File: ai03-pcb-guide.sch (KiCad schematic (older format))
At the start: 24 parts, among them SW1 SW_Push, U1 ATmega32U4-AU, Y1 16MHz

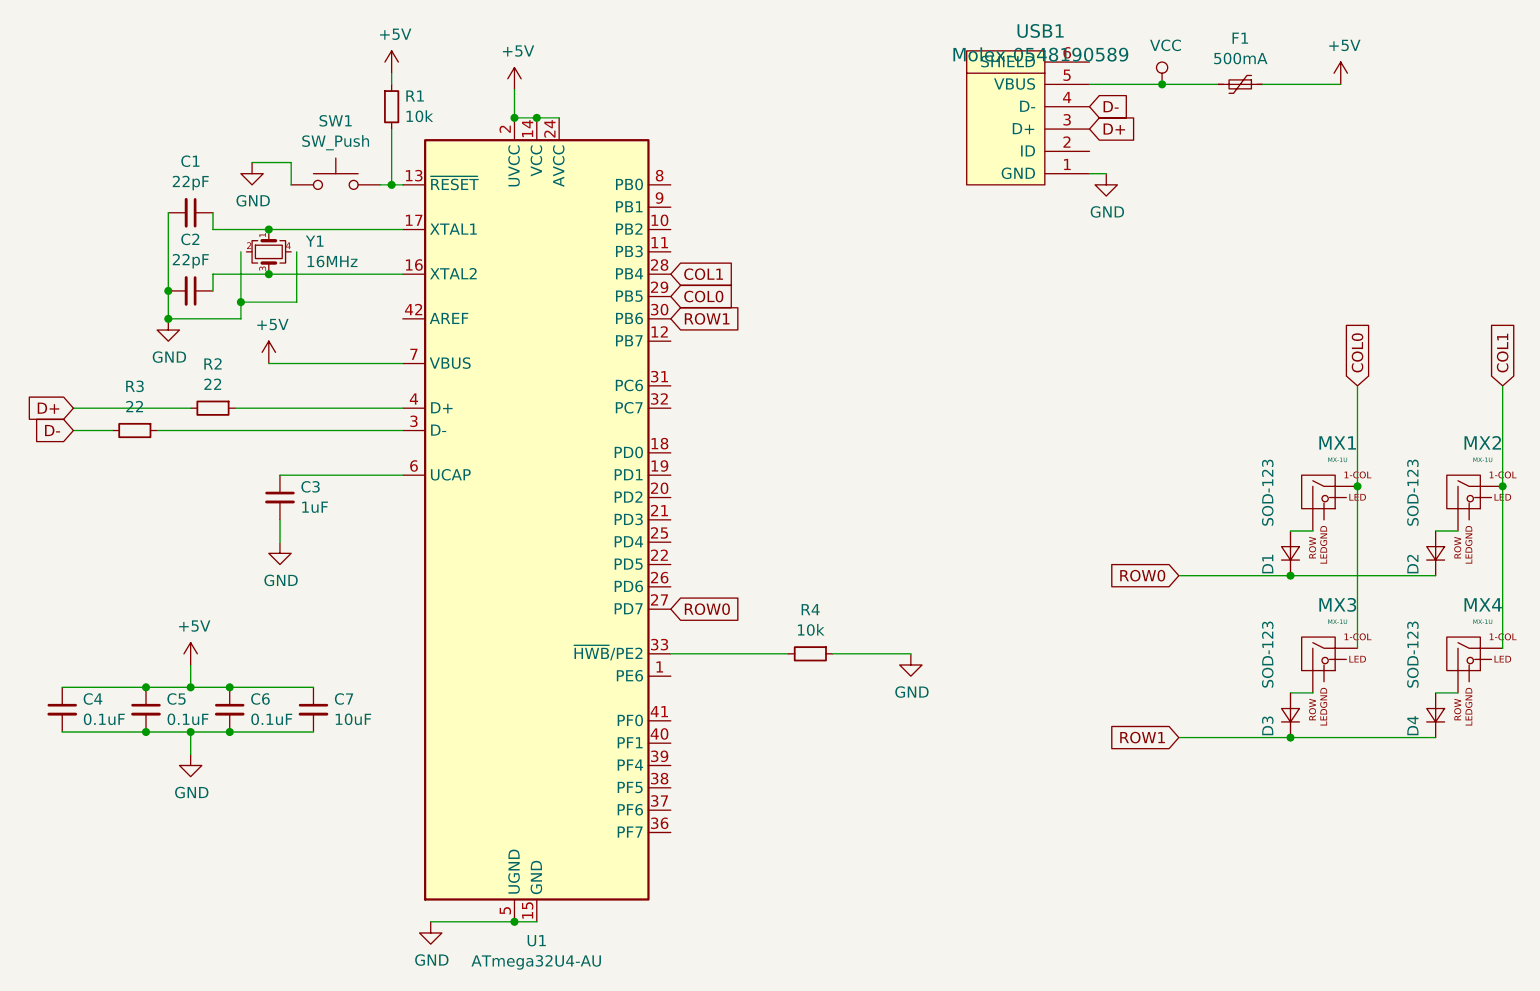
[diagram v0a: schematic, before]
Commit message: Update to KiCad 5.1.2 guide data
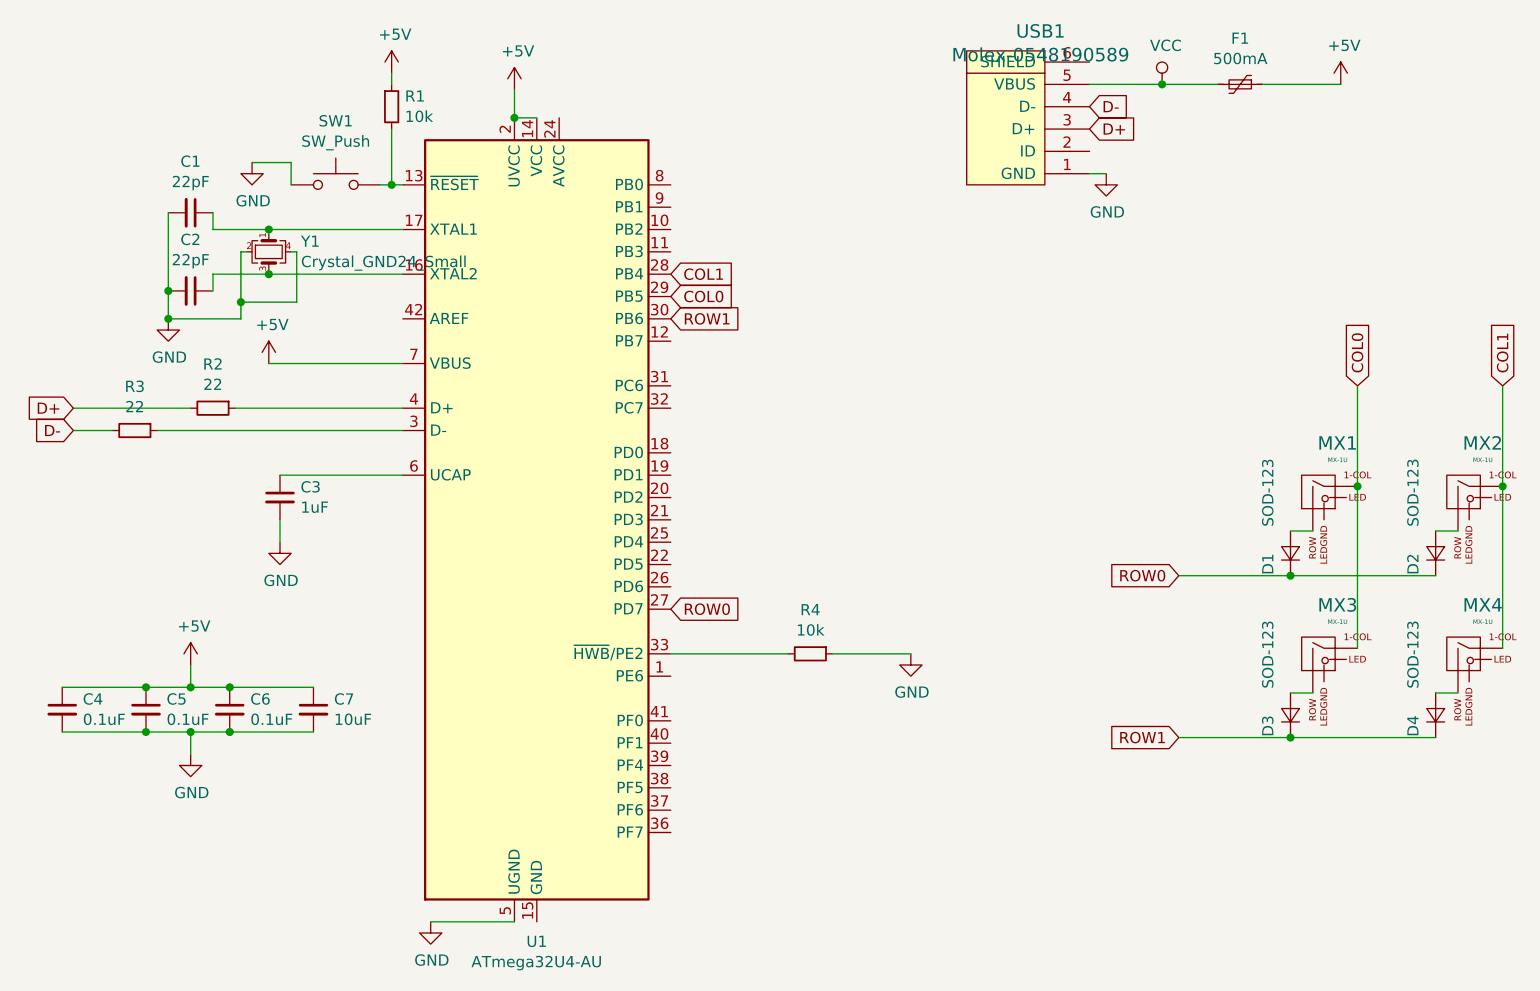
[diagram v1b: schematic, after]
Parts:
- Y1: value 16MHz -> Crystal_GND24_Small
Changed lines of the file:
@@
 EESchema Schematic File Version 4
-EELAYER 26 0
+LIBS:ai03-pcb-guide-cache
+EELAYER 29 0
 EELAYER END
 $Descr A4 11693 8268
@@
 $EndDescr
 $Comp
-L MCU_Microchip_ATmega:ATmega32U4-AU U1
-U 1 1 5C33F15A
-P 3650 3625
-F 0 "U1" H 3650 1739 50  0000 C CNN
-F 1 "ATmega32U4-AU" H 3650 1648 50  0000 C CNN
-F 2 "Housings_QFP:TQFP-44_10x10mm_Pitch0.8mm" H 3650 3625 50  0001 C CIN
-F 3 "http://ww1.microchip.com/downloads/en/DeviceDoc/Atmel-7766-8-bit-AVR-ATmega16U4-32U4_Datasheet.pdf" H 3650 3625 50  0001 C CNN
-	1    3650 3625
-	1    0    0    -1
-$EndComp
-$Comp
 L power:+5V #PWR0101
 U 1 1 5C33F300
@@
 Wire Wire Line
 	3550 1700 3550 1825
-Wire Wire Line
-	3550 1825 3650 1825
-Connection ~ 3550 1825
-Connection ~ 3650 1825
-Wire Wire Line
-	3650 1825 3750 1825
 $Comp
 L power:GND #PWR0102
@@
 	1    0    0    -1
 $EndComp
-Wire Wire Line
-	3175 5425 3550 5425
-Connection ~ 3550 5425
-Wire Wire Line
-	3550 5425 3650 5425
 $Comp
 L Device:R_Small R4
@@
 	2450 2925 3050 2925
 $Comp
-L Device:Crystal_GND24_Small Y1
-U 1 1 5C341379
-P 2450 2425
-F 0 "Y1" V 2404 2591 50  0000 L CNN
-F 1 "16MHz" V 2495 2591 50  0000 L CNN
-F 2 "Crystals:Crystal_SMD_3225-4pin_3.2x2.5mm" H 2450 2425 50  0001 C CNN
-F 3 "~" H 2450 2425 50  0001 C CNN
-	1    2450 2425
-	0    1    1    0
-$EndComp
-Wire Wire Line
-	2450 2325 3050 2325
-Wire Wire Line
-	3050 2525 2450 2525
-$Comp
 L Device:C_Small C1
 U 1 1 5C341D22
@@
 $EndComp
 Wire Wire Line
-	2450 2325 2200 2325
-Wire Wire Line
 	2200 2325 2200 2250
-Connection ~ 2450 2325
-Wire Wire Line
-	2450 2525 2200 2525
 Wire Wire Line
 	2200 2525 2200 2600
-Connection ~ 2450 2525
 $Comp
 L power:GND #PWR0108
@@
 Text GLabel 4250 2725 2    50   Input ~ 0
 ROW1
+Wire Wire Line
+	2550 2425 2575 2425
+Wire Wire Line
+	2350 2425 2325 2425
+$Comp
+L MCU_Microchip_ATmega:ATmega32U4-AU U1
+U 1 1 5CEB8A23
+P 3650 3625
+F 0 "U1" H 3650 1736 50  0000 C CNN
+F 1 "ATmega32U4-AU" H 3650 1645 50  0000 C CNN
+F 2 "Housings_QFP:TQFP-44_10x10mm_Pitch0.8mm" H 3650 3625 50  0001 C CIN
+F 3 "http://ww1.microchip.com/downloads/en/DeviceDoc/Atmel-7766-8-bit-AVR-ATmega16U4-32U4_Datasheet.pdf" H 3650 3625 50  0001 C CNN
+	1    3650 3625
+	1    0    0    -1
+$EndComp
+Wire Wire Line
+	3550 1825 3650 1825
+Wire Wire Line
+	3175 5425 3550 5425
+Connection ~ 3550 1825
+Wire Wire Line
+	2200 2325 2450 2325
+Wire Wire Line
+	2200 2525 2450 2525
+$Comp
+L Device:Crystal_GND24_Small Y1
+U 1 1 5CEBCEA8
+P 2450 2425
+F 0 "Y1" V 2404 2569 50  0000 L CNN
+F 1 "Crystal_GND24_Small" V 2495 2569 50  0000 L CNN
+F 2 "Crystals:Crystal_SMD_3225-4pin_3.2x2.5mm" H 2450 2425 50  0001 C CNN
+F 3 "~" H 2450 2425 50  0001 C CNN
+	1    2450 2425
+	0    1    1    0
+$EndComp
+Connection ~ 2450 2525
+Wire Wire Line
+	2450 2525 3050 2525
+Connection ~ 2450 2325
+Wire Wire Line
+	2450 2325 3050 2325
 $EndSCHEMATC

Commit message: Progress
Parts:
- removed MX1, MX2, MX3, MX4: MX-1U, MX_Alps_Hybrid:MX-1U, symbol MX_Alps_Hybrids:MX-1U
- added MX? (x4): MX-NoLED, symbol MX_Alps_Hybrid:MX-NoLED
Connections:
- net COL0: now also MX?.1 (COL), MX?.1 (COL)
- net COL1: now also MX?.1 (COL), MX?.1 (COL)
- net at D1.2 (A): now also MX?.2 (ROW)
- net at D2.2 (A): now also MX?.2 (ROW)
- net at D3.2 (A): now also MX?.2 (ROW)
- net at D4.2 (A): now also MX?.2 (ROW)
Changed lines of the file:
@@
 	6200 2075 6125 2075
-$Comp
-L MX_Alps_Hybrids:MX-1U MX1
-U 1 1 5C34B436
-P 7150 3500
-F 0 "MX1" H 7236 3717 60  0000 C CNN
-F 1 "MX-1U" H 7236 3643 20  0000 C CNN
-F 2 "MX_Alps_Hybrid:MX-1U" H 7125 3475 60  0001 C CNN
-F 3 "" H 7125 3475 60  0001 C CNN
-	1    7150 3500
-	1    0    0    -1
-$EndComp
 $Comp
 L Device:D_Small D1
@@
 	7025 3675 7125 3675
 $Comp
-L MX_Alps_Hybrids:MX-1U MX2
-U 1 1 5C34C49C
-P 7800 3500
-F 0 "MX2" H 7886 3717 60  0000 C CNN
-F 1 "MX-1U" H 7886 3643 20  0000 C CNN
-F 2 "MX_Alps_Hybrid:MX-1U" H 7775 3475 60  0001 C CNN
-F 3 "" H 7775 3475 60  0001 C CNN
-	1    7800 3500
-	1    0    0    -1
-$EndComp
-$Comp
 L Device:D_Small D2
 U 1 1 5C34C4A3
@@
 	7675 3675 7775 3675
 $Comp
-L MX_Alps_Hybrids:MX-1U MX3
-U 1 1 5C34D1F8
-P 7150 4225
-F 0 "MX3" H 7236 4442 60  0000 C CNN
-F 1 "MX-1U" H 7236 4368 20  0000 C CNN
-F 2 "MX_Alps_Hybrid:MX-1U" H 7125 4200 60  0001 C CNN
-F 3 "" H 7125 4200 60  0001 C CNN
-	1    7150 4225
-	1    0    0    -1
-$EndComp
-$Comp
 L Device:D_Small D3
 U 1 1 5C34D1FF
@@
 Wire Wire Line
 	7025 4400 7125 4400
-$Comp
-L MX_Alps_Hybrids:MX-1U MX4
-U 1 1 5C34D207
-P 7800 4225
-F 0 "MX4" H 7886 4442 60  0000 C CNN
-F 1 "MX-1U" H 7886 4368 20  0000 C CNN
-F 2 "MX_Alps_Hybrid:MX-1U" H 7775 4200 60  0001 C CNN
-F 3 "" H 7775 4200 60  0001 C CNN
-	1    7800 4225
-	1    0    0    -1
-$EndComp
 $Comp
 L Device:D_Small D4
@@
 Wire Wire Line
 	7025 4600 6525 4600
-Wire Wire Line
-	7325 4200 7325 3475
-Connection ~ 7325 3475
-Wire Wire Line
-	7325 3475 7325 3025
-Wire Wire Line
-	7975 4200 7975 3475
-Connection ~ 7975 3475
-Wire Wire Line
-	7975 3475 7975 3025
 Text GLabel 7325 3025 1    50   Input ~ 0
 COL0
@@
 Wire Wire Line
 	2450 2325 3050 2325
+Wire Wire Line
+	7325 3025 7325 3475
+Wire Wire Line
+	7975 3025 7975 3475
+$Comp
+L MX_Alps_Hybrid:MX-NoLED MX?
+U 1 1 5D099790
+P 7175 3525
+F 0 "MX?" H 7208 3748 60  0000 C CNN
+F 1 "MX-NoLED" H 7208 3674 20  0000 C CNN
+F 2 "" H 6550 3500 60  0001 C CNN
+F 3 "" H 6550 3500 60  0001 C CNN
+	1    7175 3525
+	1    0    0    -1
+$EndComp
+Connection ~ 7325 3475
+Wire Wire Line
+	7325 3475 7325 4200
+$Comp
+L MX_Alps_Hybrid:MX-NoLED MX?
+U 1 1 5D09A176
+P 7825 3525
+F 0 "MX?" H 7858 3748 60  0000 C CNN
+F 1 "MX-NoLED" H 7858 3674 20  0000 C CNN
+F 2 "" H 7200 3500 60  0001 C CNN
+F 3 "" H 7200 3500 60  0001 C CNN
+	1    7825 3525
+	1    0    0    -1
+$EndComp
+Connection ~ 7975 3475
+Wire Wire Line
+	7975 3475 7975 4200
+$Comp
+L MX_Alps_Hybrid:MX-NoLED MX?
+U 1 1 5D09AA2F
+P 7175 4250
+F 0 "MX?" H 7208 4473 60  0000 C CNN
+F 1 "MX-NoLED" H 7208 4399 20  0000 C CNN
+F 2 "" H 6550 4225 60  0001 C CNN
+F 3 "" H 6550 4225 60  0001 C CNN
+	1    7175 4250
+	1    0    0    -1
+$EndComp
+$Comp
+L MX_Alps_Hybrid:MX-NoLED MX?
+U 1 1 5D09B9B4
+P 7825 4250
+F 0 "MX?" H 7858 4473 60  0000 C CNN
+F 1 "MX-NoLED" H 7858 4399 20  0000 C CNN
+F 2 "" H 7200 4225 60  0001 C CNN
+F 3 "" H 7200 4225 60  0001 C CNN
+	1    7825 4250
+	1    0    0    -1
+$EndComp
 $EndSCHEMATC

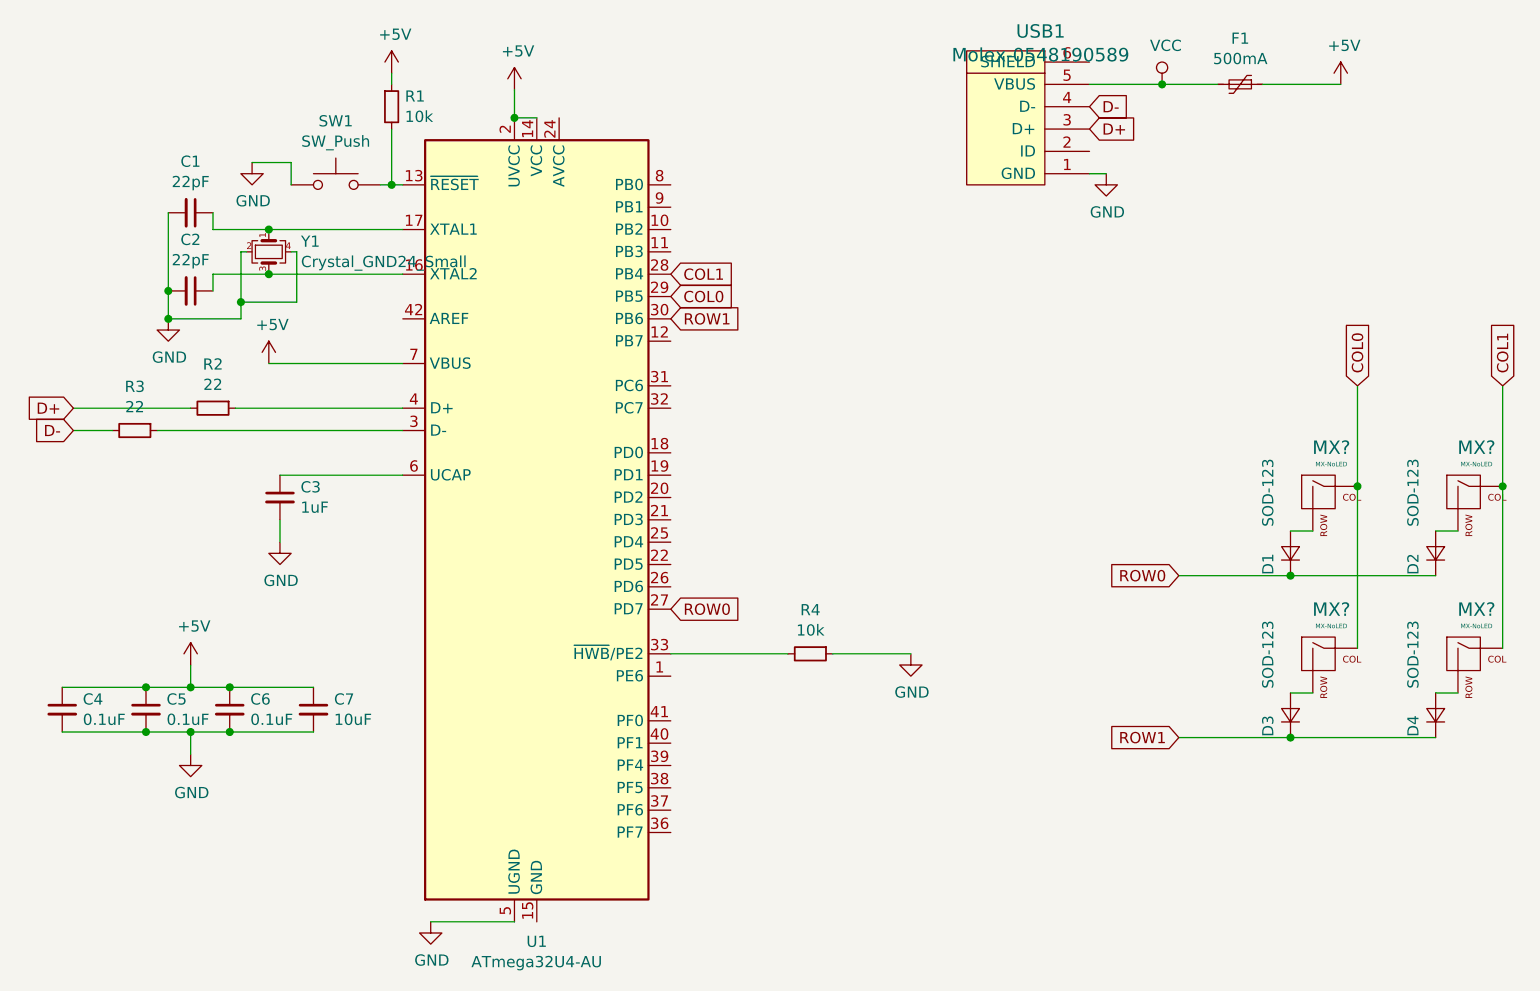
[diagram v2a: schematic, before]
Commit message: Update PCB for revised guide
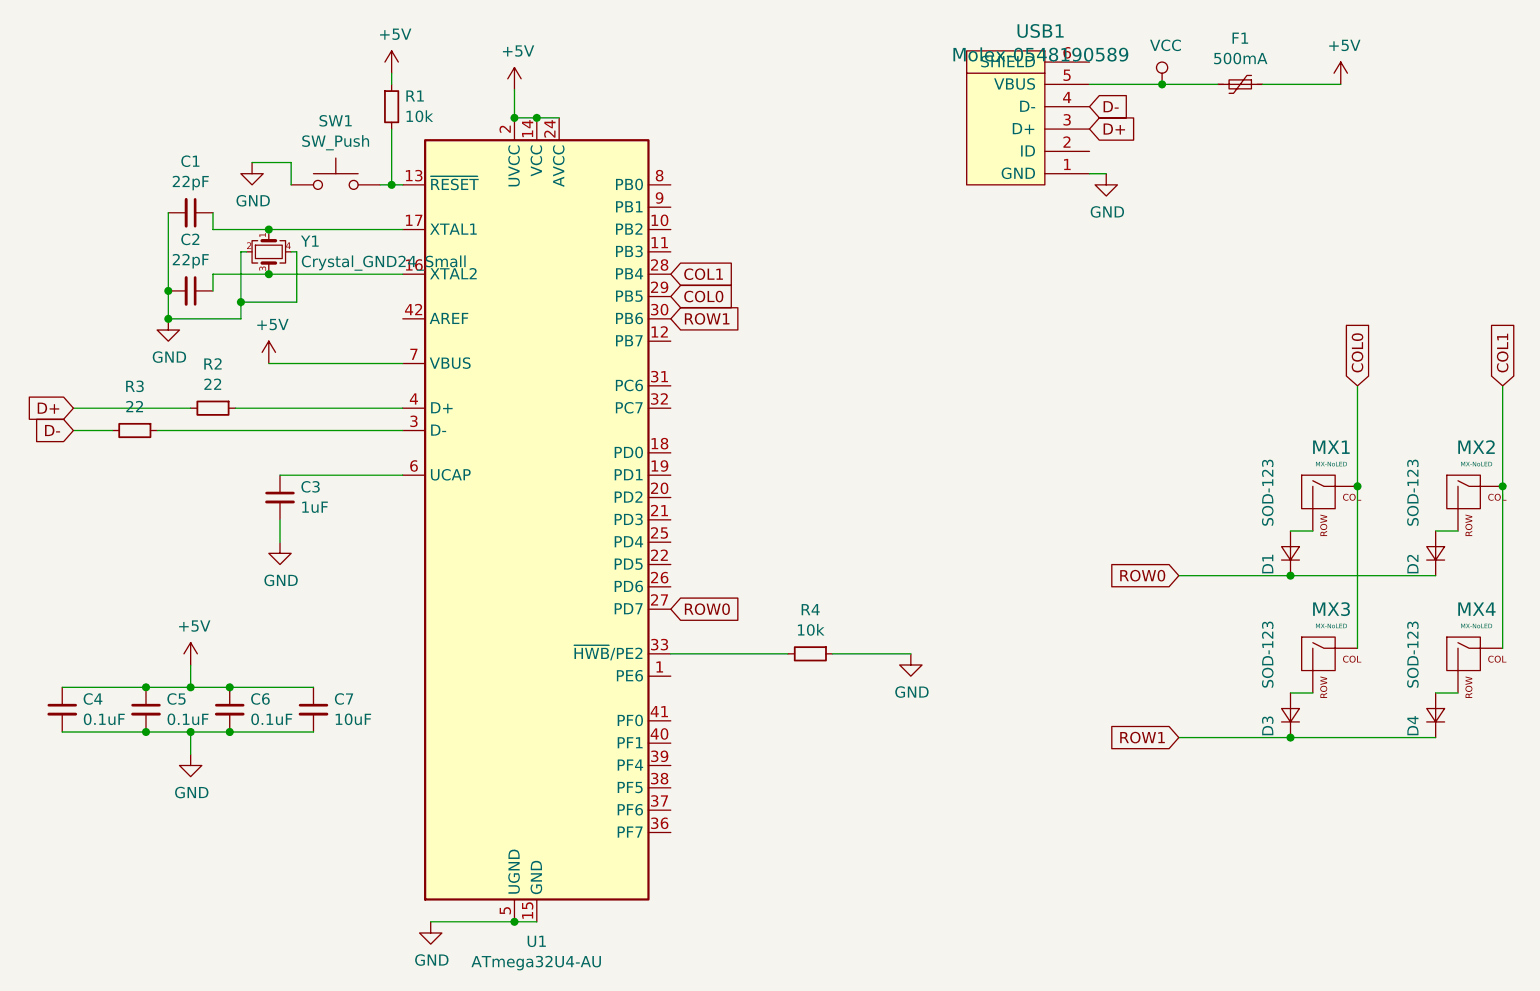
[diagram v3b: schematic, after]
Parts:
- MX1, MX2, MX3, MX4: renamed from MX?; footprint (none) -> MX_Alps_Hybrid:MX-1U
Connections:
- net +5V: now also U1.24 (AVCC), U1.44 (AVCC)
- net GND: now also U1.15 (GND), U1.23 (GND), U1.35 (GND), U1.43 (GND)
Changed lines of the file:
@@
 Wire Wire Line
 	7675 3875 7025 3875
-Connection ~ 7025 3875
 Wire Wire Line
 	7025 3875 6525 3875
 Wire Wire Line
 	7675 4600 7025 4600
-Connection ~ 7025 4600
 Wire Wire Line
 	7025 4600 6525 4600
@@
 	7975 3025 7975 3475
 $Comp
-L MX_Alps_Hybrid:MX-NoLED MX?
+L MX_Alps_Hybrid:MX-NoLED MX1
 U 1 1 5D099790
 P 7175 3525
-F 0 "MX?" H 7208 3748 60  0000 C CNN
+F 0 "MX1" H 7208 3748 60  0000 C CNN
 F 1 "MX-NoLED" H 7208 3674 20  0000 C CNN
-F 2 "" H 6550 3500 60  0001 C CNN
+F 2 "MX_Alps_Hybrid:MX-1U" H 6550 3500 60  0001 C CNN
 F 3 "" H 6550 3500 60  0001 C CNN
 	1    7175 3525
 	1    0    0    -1
 $EndComp
-Connection ~ 7325 3475
 Wire Wire Line
 	7325 3475 7325 4200
 $Comp
-L MX_Alps_Hybrid:MX-NoLED MX?
+L MX_Alps_Hybrid:MX-NoLED MX2
 U 1 1 5D09A176
 P 7825 3525
-F 0 "MX?" H 7858 3748 60  0000 C CNN
+F 0 "MX2" H 7858 3748 60  0000 C CNN
 F 1 "MX-NoLED" H 7858 3674 20  0000 C CNN
-F 2 "" H 7200 3500 60  0001 C CNN
+F 2 "MX_Alps_Hybrid:MX-1U" H 7200 3500 60  0001 C CNN
 F 3 "" H 7200 3500 60  0001 C CNN
 	1    7825 3525
 	1    0    0    -1
 $EndComp
-Connection ~ 7975 3475
 Wire Wire Line
 	7975 3475 7975 4200
 $Comp
-L MX_Alps_Hybrid:MX-NoLED MX?
+L MX_Alps_Hybrid:MX-NoLED MX3
 U 1 1 5D09AA2F
 P 7175 4250
-F 0 "MX?" H 7208 4473 60  0000 C CNN
+F 0 "MX3" H 7208 4473 60  0000 C CNN
 F 1 "MX-NoLED" H 7208 4399 20  0000 C CNN
-F 2 "" H 6550 4225 60  0001 C CNN
+F 2 "MX_Alps_Hybrid:MX-1U" H 6550 4225 60  0001 C CNN
 F 3 "" H 6550 4225 60  0001 C CNN
 	1    7175 4250
@@
 $EndComp
 $Comp
-L MX_Alps_Hybrid:MX-NoLED MX?
+L MX_Alps_Hybrid:MX-NoLED MX4
 U 1 1 5D09B9B4
 P 7825 4250
-F 0 "MX?" H 7858 4473 60  0000 C CNN
+F 0 "MX4" H 7858 4473 60  0000 C CNN
 F 1 "MX-NoLED" H 7858 4399 20  0000 C CNN
-F 2 "" H 7200 4225 60  0001 C CNN
+F 2 "MX_Alps_Hybrid:MX-1U" H 7200 4225 60  0001 C CNN
 F 3 "" H 7200 4225 60  0001 C CNN
 	1    7825 4250
 	1    0    0    -1
 $EndComp
+Connection ~ 7325 3475
+Connection ~ 7975 3475
+Connection ~ 7025 3875
+Connection ~ 7025 4600
+Wire Wire Line
+	3750 1825 3650 1825
+Connection ~ 3650 1825
+Wire Wire Line
+	3650 5425 3550 5425
+Connection ~ 3550 5425
 $EndSCHEMATC
